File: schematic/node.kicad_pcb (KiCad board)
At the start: 2 copper layers, 12 parts, among them IC1 ATMEGA328P-P, P1 NRF24L01, P2 CONN_01X06, P3 CONN_01X02

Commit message: add kicad design files
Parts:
- removed C5: 0.1 uF, Capacitors_ThroughHole:C_Disc_D3_P2.5
- added P4: HEADER_LEFT, Pin_Headers:Pin_Header_Straight_1x08, F.Cu at (150.2, 127.0)
- added P5: HEADER_RIGHT, Pin_Headers:Pin_Header_Straight_1x05, F.Cu at (183.8, 144.8)
- added REF**: 1pin, Connect:1pin, F.Cu at (187.0, 88.0)
- added REF**: 1pin, Connect:1pin, F.Cu at (147.0, 88.0)
- added REF**: Symbol_OSHW-Logo_SilkScreen, Symbols:Symbol_OSHW-Logo_SilkScreen, F.Cu at (184.5, 99.5)
- C2: value 0.1 uF -> 4.7 uF; footprint Capacitors_ThroughHole:C_Disc_D3_P2.5 -> Capacitors_ThroughHole:C_Radial_D5_L11_P2.5
- C3: value 4.7 uF -> 0.1 uF; footprint Capacitors_ThroughHole:C_Radial_D5_L6_P2.5 -> Capacitors_ThroughHole:C_Disc_D3_P2.5
- P2: value CONN_01X06 -> FTDI
- P3: value CONN_01X02 -> POWER
- moved P3 47.1 mm to (158.0, 91.0), turned to 270 degrees
- moved C3 46.6 mm to (156.0, 101.0), turned to 90 degrees
- moved C2 26.7 mm to (159.0, 144.0), turned to 270 degrees
- moved R2 26.4 mm to (173.8, 132.2), turned to 90 degrees
- moved C4 18.7 mm to (172.5, 116.8), turned to 0 degrees
- moved P2 10.4 mm to (181.0, 91.0)
- moved R1 10.1 mm to (155.8, 110.0), turned to 90 degrees
- moved P1 5.58 mm to (165.0, 146.0)
- moved C1 4.48 mm to (175.8, 121.8)
- moved R3 2.46 mm to (174.0, 105.2)
- moved IC1 1.34 mm to (161.0, 104.0)
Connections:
- net /RX renamed RX
- net /TX renamed TX
- C1 pad 2: +3V3 -> Net-(C1-Pad2)
- C2 pad 1: GND -> +3V3
- C2 pad 2: Net-(C2-Pad2) -> GND
- C3 pad 1: +3V3 -> Net-(C3-Pad1)
- C3 pad 2: GND -> DTR
- C4 pad 2: /DTR -> GND
- IC1 pad 1: Net-(C4-Pad1) -> Net-(C3-Pad1)
- IC1 pad 10: Net-(IC1-Pad10) -> PB7
- IC1 pad 11: Net-(IC1-Pad11) -> PD5
- IC1 pad 12: Net-(IC1-Pad12) -> PD6
- IC1 pad 13: Net-(IC1-Pad13) -> PD7
- IC1 pad 14: Net-(IC1-Pad14) -> PB0
- IC1 pad 21: Net-(C2-Pad2) -> Net-(C1-Pad2)
- IC1 pad 23: Net-(C5-Pad1) -> Net-(C4-Pad1)
- IC1 pad 24: Net-(IC1-Pad24) -> PC1
- IC1 pad 25: Net-(IC1-Pad25) -> PC2
- IC1 pad 26: Net-(IC1-Pad26) -> PC3
- IC1 pad 27: Net-(IC1-Pad27) -> PC4
- IC1 pad 28: Net-(IC1-Pad28) -> PC5
- IC1 pad 4: Net-(IC1-Pad4) -> PD2
- IC1 pad 5: Net-(IC1-Pad5) -> PD3
- IC1 pad 9: Net-(IC1-Pad9) -> PB6
- P1 pad 3: Net-(IC1-Pad9) -> Net-(IC1-Pad15)
- P1 pad 8: Net-(IC1-Pad4) -> Net-(IC1-Pad6)
- P2 pad 6: /DTR -> DTR
- R1 pad 2: Net-(C4-Pad1) -> Net-(C3-Pad1)
- R2 pad 2: Net-(C5-Pad1) -> Net-(C4-Pad1)
- R3 pad 1: Net-(C5-Pad1) -> Net-(C4-Pad1)
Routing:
- net +3V3: track 122.7 -> 0.00 mm, vias 4 -> 0
- net GND: track 102.2 -> 0.00 mm
- net Net-(IC1-Pad4): track 94.6 -> 0.00 mm, vias 4 -> 0
- net PC2: track 0.00 -> 58.2 mm
- net Net-(IC1-Pad9): track 49.8 -> 0.00 mm, vias 2 -> 0
- net PC1: track 0.00 -> 43.5 mm
- net PC5: track 0.00 -> 37.7 mm
- net PC4: track 0.00 -> 36.9 mm
- net PC3: track 0.00 -> 36.9 mm
- net Net-(IC1-Pad6): track 0.00 -> 32.0 mm
- net Net-(IC1-Pad19): track 53.7 -> 28.0 mm, vias 2 -> 0
- net PD3: track 0.00 -> 20.0 mm
- net PD2: track 0.00 -> 19.8 mm
- net Net-(IC1-Pad15): track 0.00 -> 18.9 mm, vias 0 -> 1
- net DTR: track 0.00 -> 15.4 mm
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- added copper zone on F.Cu, net +3V3
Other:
- board outline added: 50 x 70 mm
- net class Default: clearance 0.5 -> 0.35; trace_width 0.6 -> 0.5; via_dia 1.3 -> 0.6; via_drill 0.9 -> 0.4
- rule pad_to_mask_clearance: 0.2 -> 0
- rule trace_clearance: 0.5 -> 0.35
- board text added: "01.2016 by szaffarano"
- board text added: "WiZaNO v1.0"

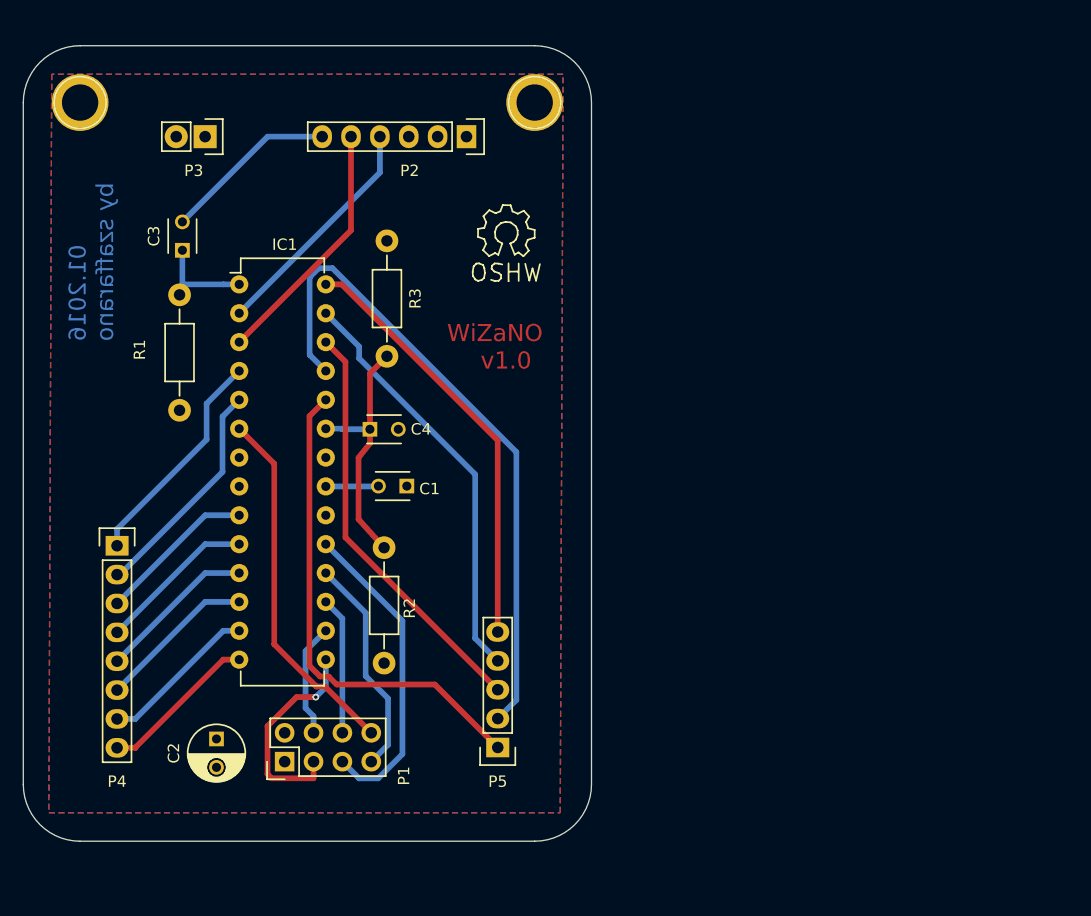
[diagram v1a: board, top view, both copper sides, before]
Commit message: refactoring in pcb layout
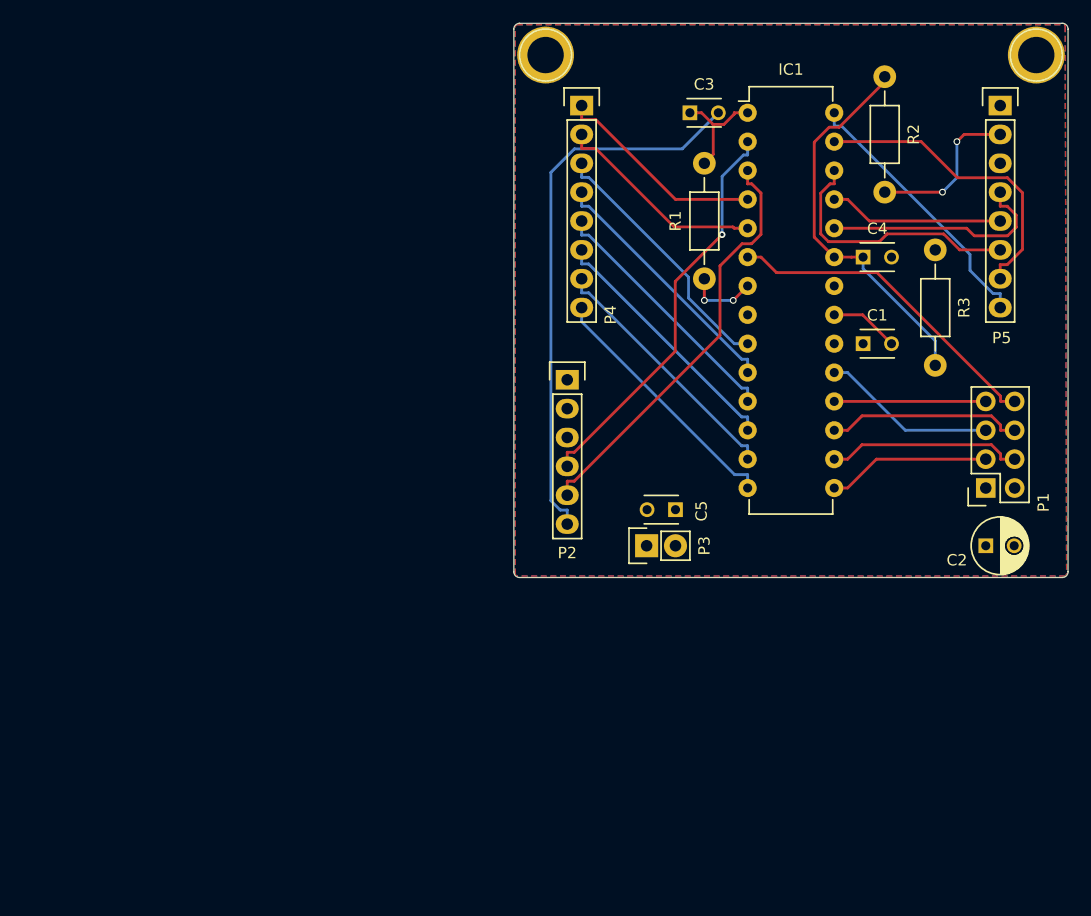
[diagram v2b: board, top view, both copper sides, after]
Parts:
- removed REF** (x2): 1pin, Connect:1pin
- removed REF**: Symbol_OSHW-Logo_SilkScreen, Symbols:Symbol_OSHW-Logo_SilkScreen
- added C5: 0.1 uF, Capacitors_ThroughHole:C_Disc_D3_P2.5, F.Cu at (199.4, 123.8)
- added REF1: 1pin, Connect:1pin, F.Cu at (188.0, 83.8)
- added REF2: 1pin, Connect:1pin, F.Cu at (231.1, 83.8)
- C3: value 0.1 uF -> C
- P1: footprint Pin_Headers:Pin_Header_Straight_2x04 -> Socket_Strips:Socket_Strip_Straight_2x04
- P2: value FTDI -> CONN_01X06
- P3: value POWER -> CONN_01X02
- P5: footprint Pin_Headers:Pin_Header_Straight_1x05 -> Pin_Headers:Pin_Header_Straight_1x08
- moved P5 71.7 mm to (228.0, 88.3), turned to 0 degrees
- moved C2 69.8 mm to (226.7, 127.0), turned to 0 degrees
- moved P1 66.2 mm to (226.7, 121.9)
- moved R2 60.5 mm to (217.8, 90.8)
- moved P4 56.3 mm to (191.1, 88.3)
- moved P3 53.0 mm to (196.8, 127.0), turned to 90 degrees
- moved R3 48.3 mm to (222.2, 106.0)
- moved R1 47.6 mm to (201.9, 98.4)
- moved IC1 47.2 mm to (205.7, 88.9)
- moved C3 46.3 mm to (200.7, 88.9), turned to 0 degrees
- moved C4 46.0 mm to (215.9, 101.6)
- moved C1 42.1 mm to (215.9, 109.2), turned to 0 degrees
- moved P2 23.2 mm to (189.9, 112.4), turned to 0 degrees
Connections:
- P5 pad 1: PC1 -> +3V3
- P5 pad 2: PC2 -> +3V3
- P5 pad 3: PC3 -> GND
- P5 pad 4: PC4 -> PC1
- P5 pad 5: PC5 -> PC2
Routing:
- net PC2: track 58.2 -> 15.4 mm
- net DTR: track 15.4 -> 48.8 mm
- net PC1: track 43.5 -> 20.6 mm
- net +3V3: track 0.00 -> 20.4 mm, vias 0 -> 4
- net RX: track 20.7 -> 35.7 mm, vias 0 -> 1
- net TX: track 22.2 -> 37.2 mm
- net PC5: track 37.7 -> 23.9 mm
- net PC3: track 36.9 -> 23.2 mm
- net Net-(IC1-Pad19): track 28.0 -> 15.4 mm
- net Net-(C4-Pad1): track 22.6 -> 34.4 mm
- net PC4: track 36.9 -> 27.2 mm
- net PB6: track 14.0 -> 23.0 mm
- net PD6: track 14.0 -> 22.6 mm
- net PD5: track 14.0 -> 22.6 mm
- net PB7: track 14.0 -> 22.6 mm
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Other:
- board size 50 x 70 mm -> 48.8 x 48.8 mm
- net class Default: clearance 0.35 -> 0.25; trace_width 0.5 -> 0.25
- rule trace_clearance: 0.35 -> 0.25
- board text added: "0V"
- board text added: "3.3"
- board text added: "A1"
- board text added: "A2"
- board text added: "A3"
- board text added: "A4"
- board text added: "A5"
- board text added: "D2"
- board text added: "D3"
- board text added: "D5"
- board text added: "D6"
- board text added: "D7"
- board text added: "D8"
- board text added: "WiZaNo v1.0 01.2016"
- board text added: "X1"
- board text added: "X2"
- board text added: "by szaffarano 01.2016"
- board text removed: "01.2016 by szaffarano"
- board text removed: "WiZaNO v1.0"

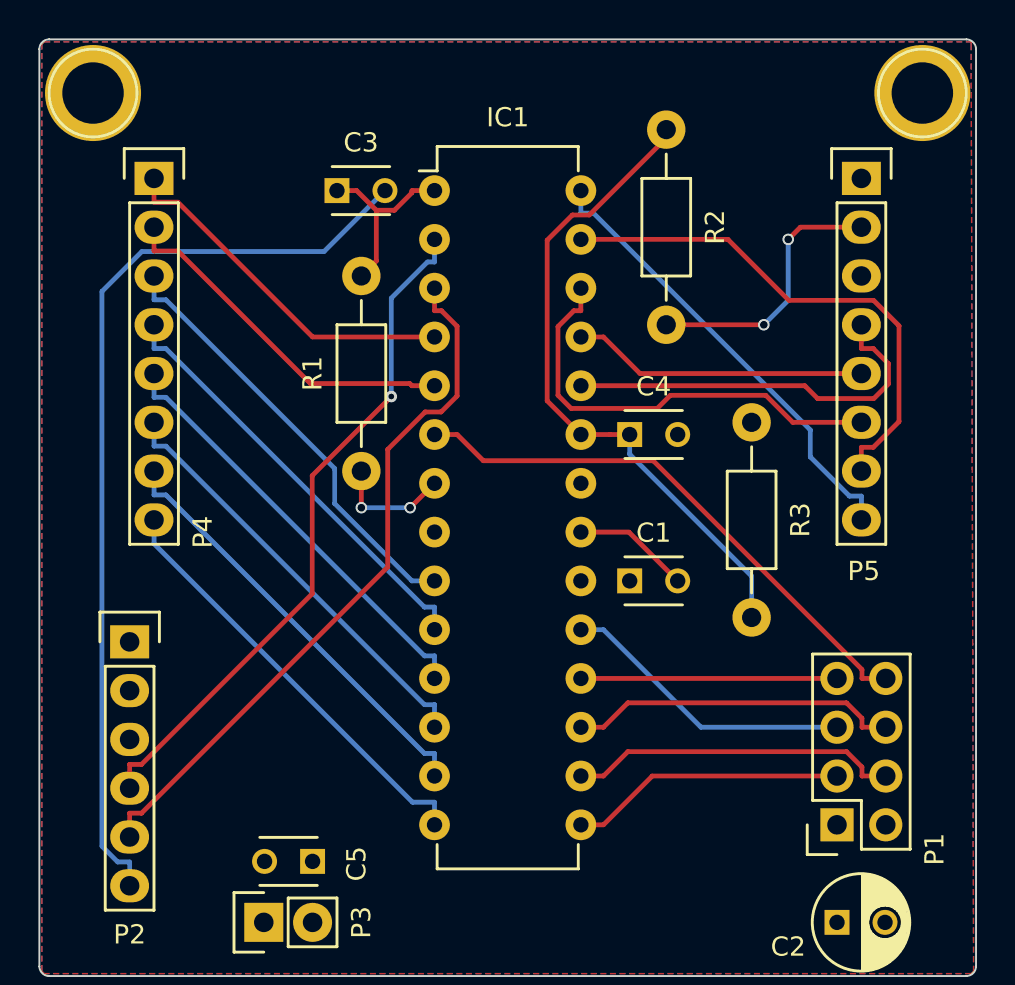
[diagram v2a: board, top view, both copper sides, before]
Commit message: fix RF irq bug in schematic
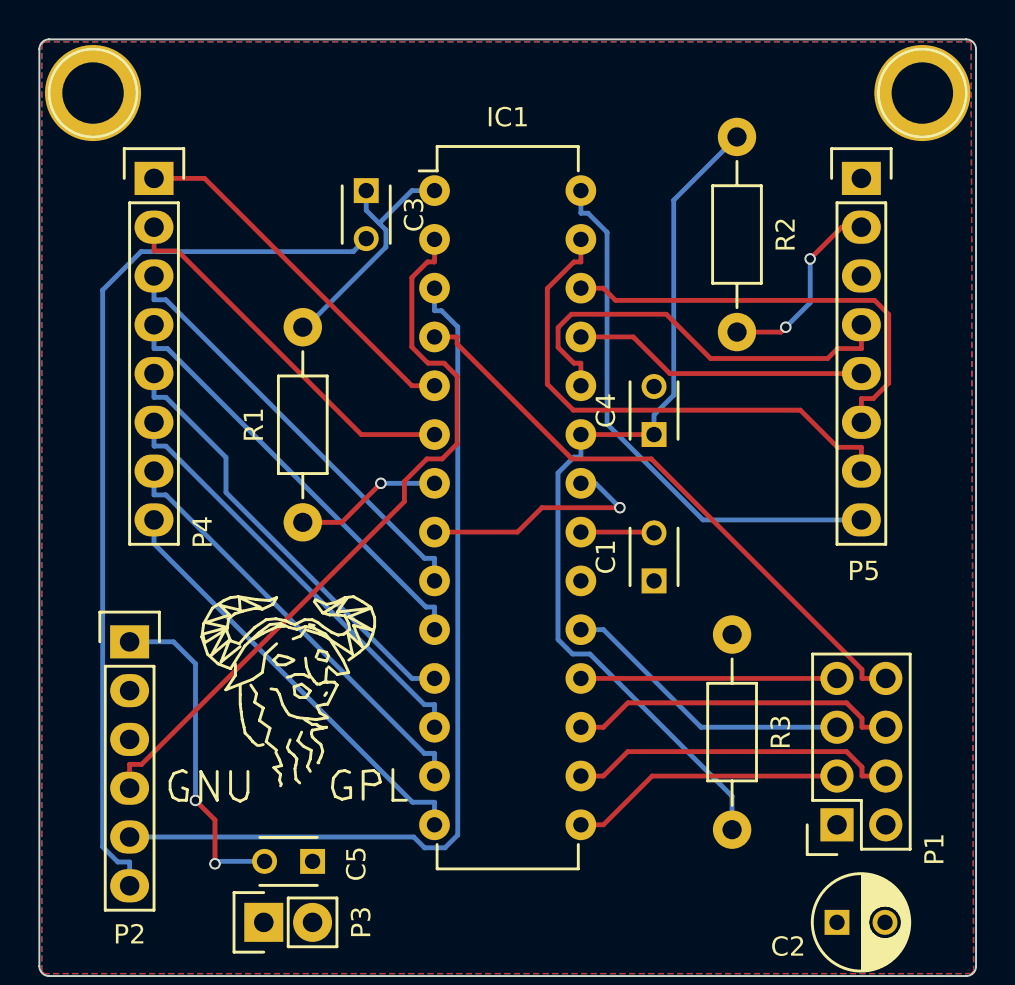
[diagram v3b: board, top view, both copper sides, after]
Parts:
- added REF3: Symbol_GNU-Logo_SilkscreenTop, Symbols:Symbol_GNU-Logo_SilkscreenTop, F.Cu at (198.4, 113.8)
- moved R3 11.1 mm to (221.2, 117.1)
- moved R1 4.05 mm to (198.9, 101.1)
- moved R2 3.70 mm to (221.5, 91.2)
- moved C3 1.52 mm to (202.2, 88.9), turned to 270 degrees
- moved C1 1.27 mm to (217.2, 109.2), turned to 90 degrees
- moved C4 1.27 mm to (217.2, 101.6), turned to 90 degrees
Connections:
- IC1 pad 4: PD2 -> Net-(IC1-Pad4)
- IC1 pad 6: Net-(IC1-Pad6) -> PD4
- P1 pad 8: Net-(IC1-Pad6) -> Net-(IC1-Pad4)
- P4 pad 1: PD2 -> PD3
- P4 pad 2: PD3 -> PD4
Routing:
- net Net-(IC1-Pad4): track 0.00 -> 31.3 mm
- net GND: track 0.00 -> 30.1 mm, vias 0 -> 3
- net Net-(IC1-Pad6): track 29.0 -> 0.00 mm
- net PD4: track 0.00 -> 19.8 mm
- net PD2: track 18.8 -> 0.00 mm
- net Net-(C4-Pad1): track 34.4 -> 46.7 mm
- net TX: track 37.2 -> 46.8 mm
- net PC5: track 23.9 -> 28.2 mm
- net Net-(C3-Pad1): track 9.74 -> 13.0 mm
- net RX: track 35.7 -> 38.6 mm, vias 1 -> 0
- net +3V3: track 20.4 -> 17.8 mm, vias 4 -> 3
- net Net-(C1-Pad2): track 6.09 -> 3.83 mm
- net DTR: track 48.8 -> 46.8 mm
- net PC1: track 20.6 -> 22.2 mm
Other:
- board text added: "D4"
- board text added: "WiZaNo v1.0"
- board text removed: "D2"
- board text removed: "WiZaNo v1.0 01.2016"
